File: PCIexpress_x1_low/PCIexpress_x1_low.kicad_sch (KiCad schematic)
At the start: 0 parts

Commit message: working to route 0.8mm pitch bga, probably not practical
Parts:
- added U1: XC7A50T-CSG325, Package_BGA:Xilinx_CSG325, symbol FPGA_Xilinx_Artix7:XC7A50T-CSG325
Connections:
- net PER0_N: now also U1.B1 (MGTPTXN3_216)
- net PER0_P: now also U1.B2 (MGTPTXP3_216)
- net PET0_N: now also U1.G3 (MGTPRXN3_216)
- net PET0_P: now also U1.G4 (MGTPRXP3_216)
- net REFCLK+: now also U1.D6 (MGTREFCLK0P_216)
- net REFCLK-: now also U1.D5 (MGTREFCLK0N_216)
- new net GND: U1.A1 (GND), U1.A11 (GND), U1.A18 (GND), U1.A5 (GND), U1.A7 (GND), U1.A8 (GND), U1.B18 (GND), U1.B3 (GND), U1.B7 (GND), U1.B8 (GND), U1.C15 (GND), U1.C2 (GND), U1.C6 (GND), U1.C7 (GND), U1.D12 (GND), U1.D3 (GND), U1.D4 (GND), U1.D7 (GND), U1.E2 (GND), U1.E6 (GND), U1.E7 (GND), U1.E9 (GND), U1.F10 (GND), U1.F16 (GND), U1.F4 (GND), U1.F6 (GND), U1.G1 (GND), U1.G11 (GND), U1.G13 (GND), U1.G5 (GND), U1.G6 (GND), U1.G7 (GND), U1.G9 (GND), U1.H10 (GND), U1.H12 (GND), U1.H3 (GND), U1.H4 (GND), U1.H5 (GND), U1.H6 (GND), U1.H8 (GND), U1.J1 (GND), U1.J11 (GND), U1.J13 (GND), U1.J17 (GND), U1.J2 (GND), U1.J3 (GND), U1.J7 (GND), U1.K12 (GND), U1.K14 (GND), U1.K4 (GND), U1.K8 (GND), U1.L1 (GND), U1.L11 (GND), U1.L13 (GND), U1.L7 (GND), U1.M12 (GND), U1.M18 (GND), U1.M8 (GND), U1.N11 (GND), U1.N13 (GND), U1.N15 (GND), U1.N5 (GND), U1.N7 (GND), U1.N9 (GND), U1.P12 (GND), U1.P2 (GND), U1.P8 (GND), U1.R9 (GND), U1.T16 (GND), U1.T6 (GND), U1.U13 (GND), U1.U3 (GND), U1.V1 (GND), U1.V10 (GND), U1.V18 (GND)

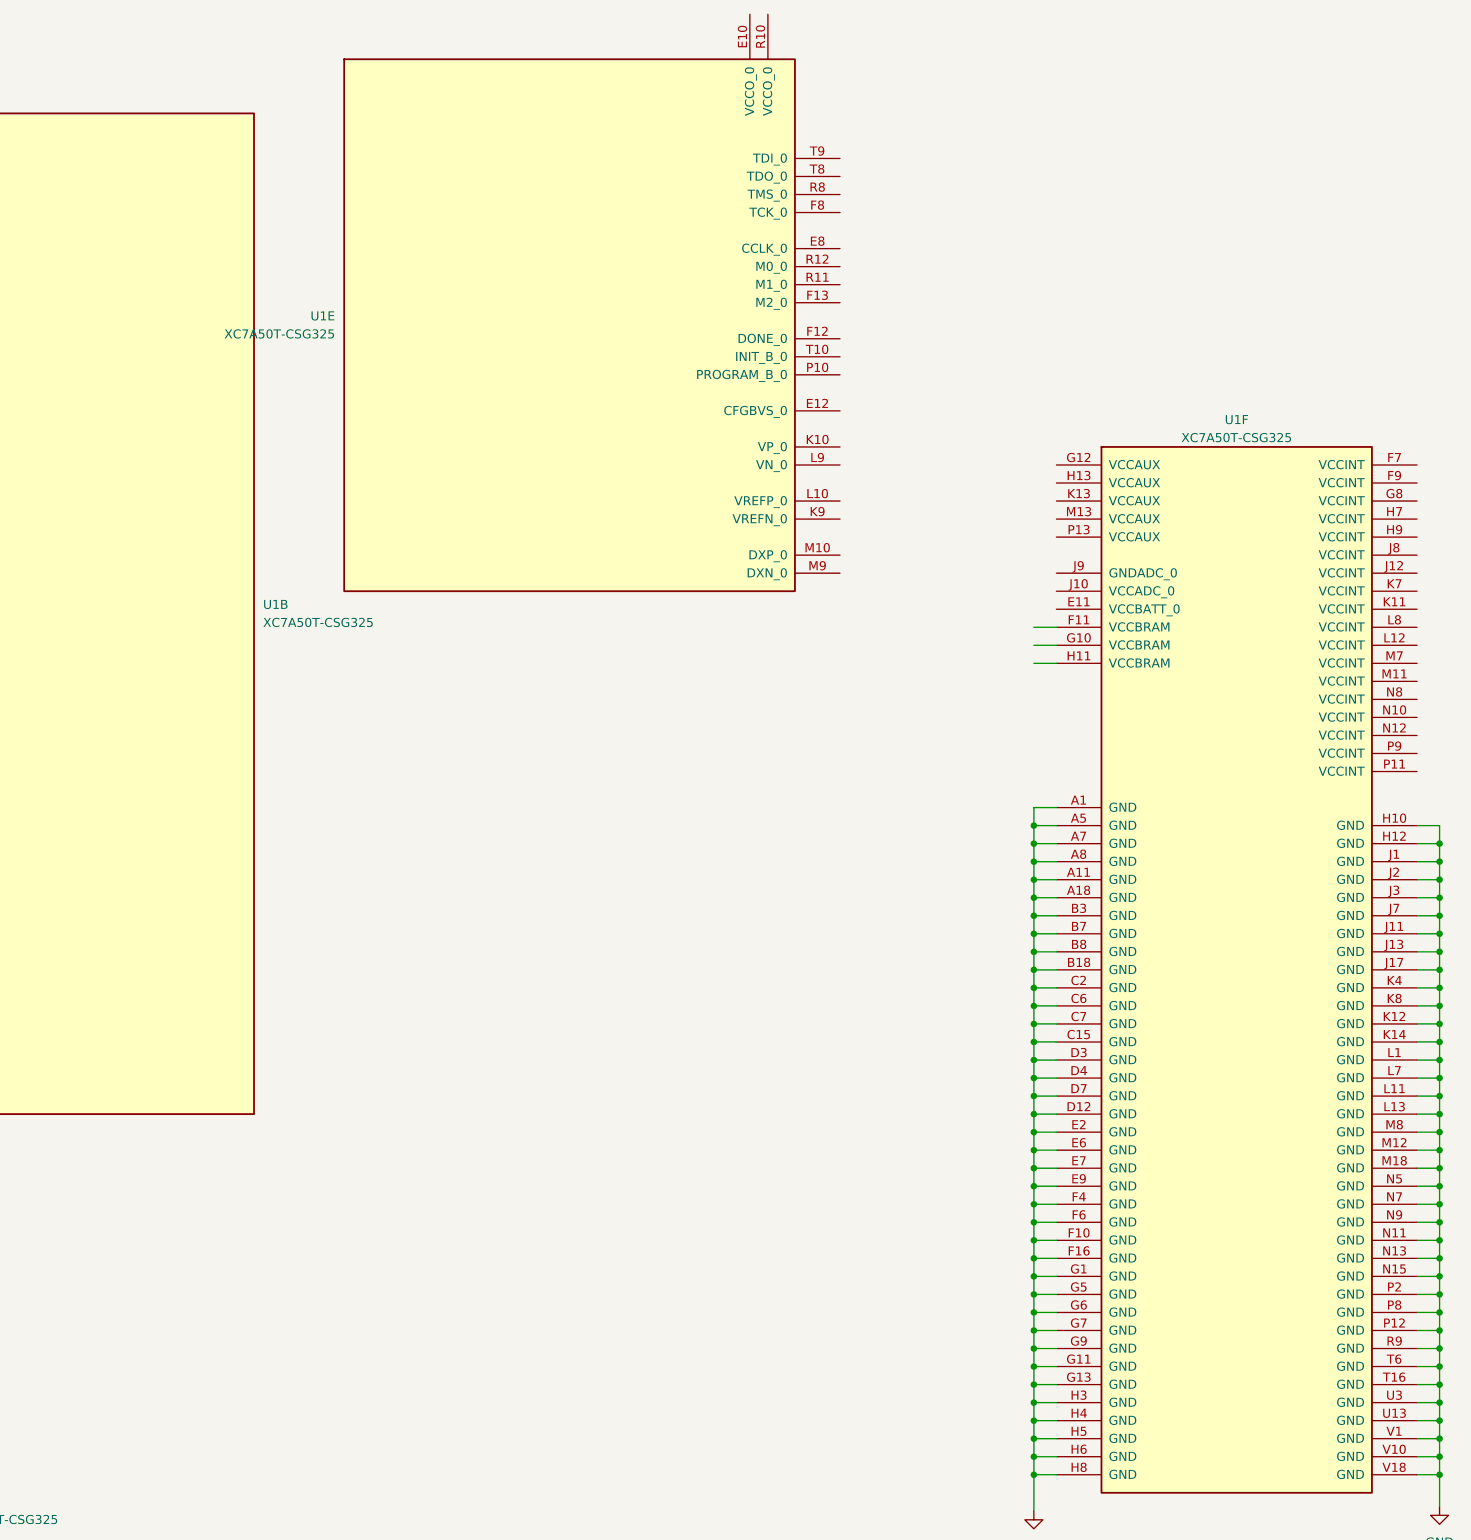
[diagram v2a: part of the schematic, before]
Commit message: looks liket the xilinx csg325 package can route in Oshpark 6 layer stackup
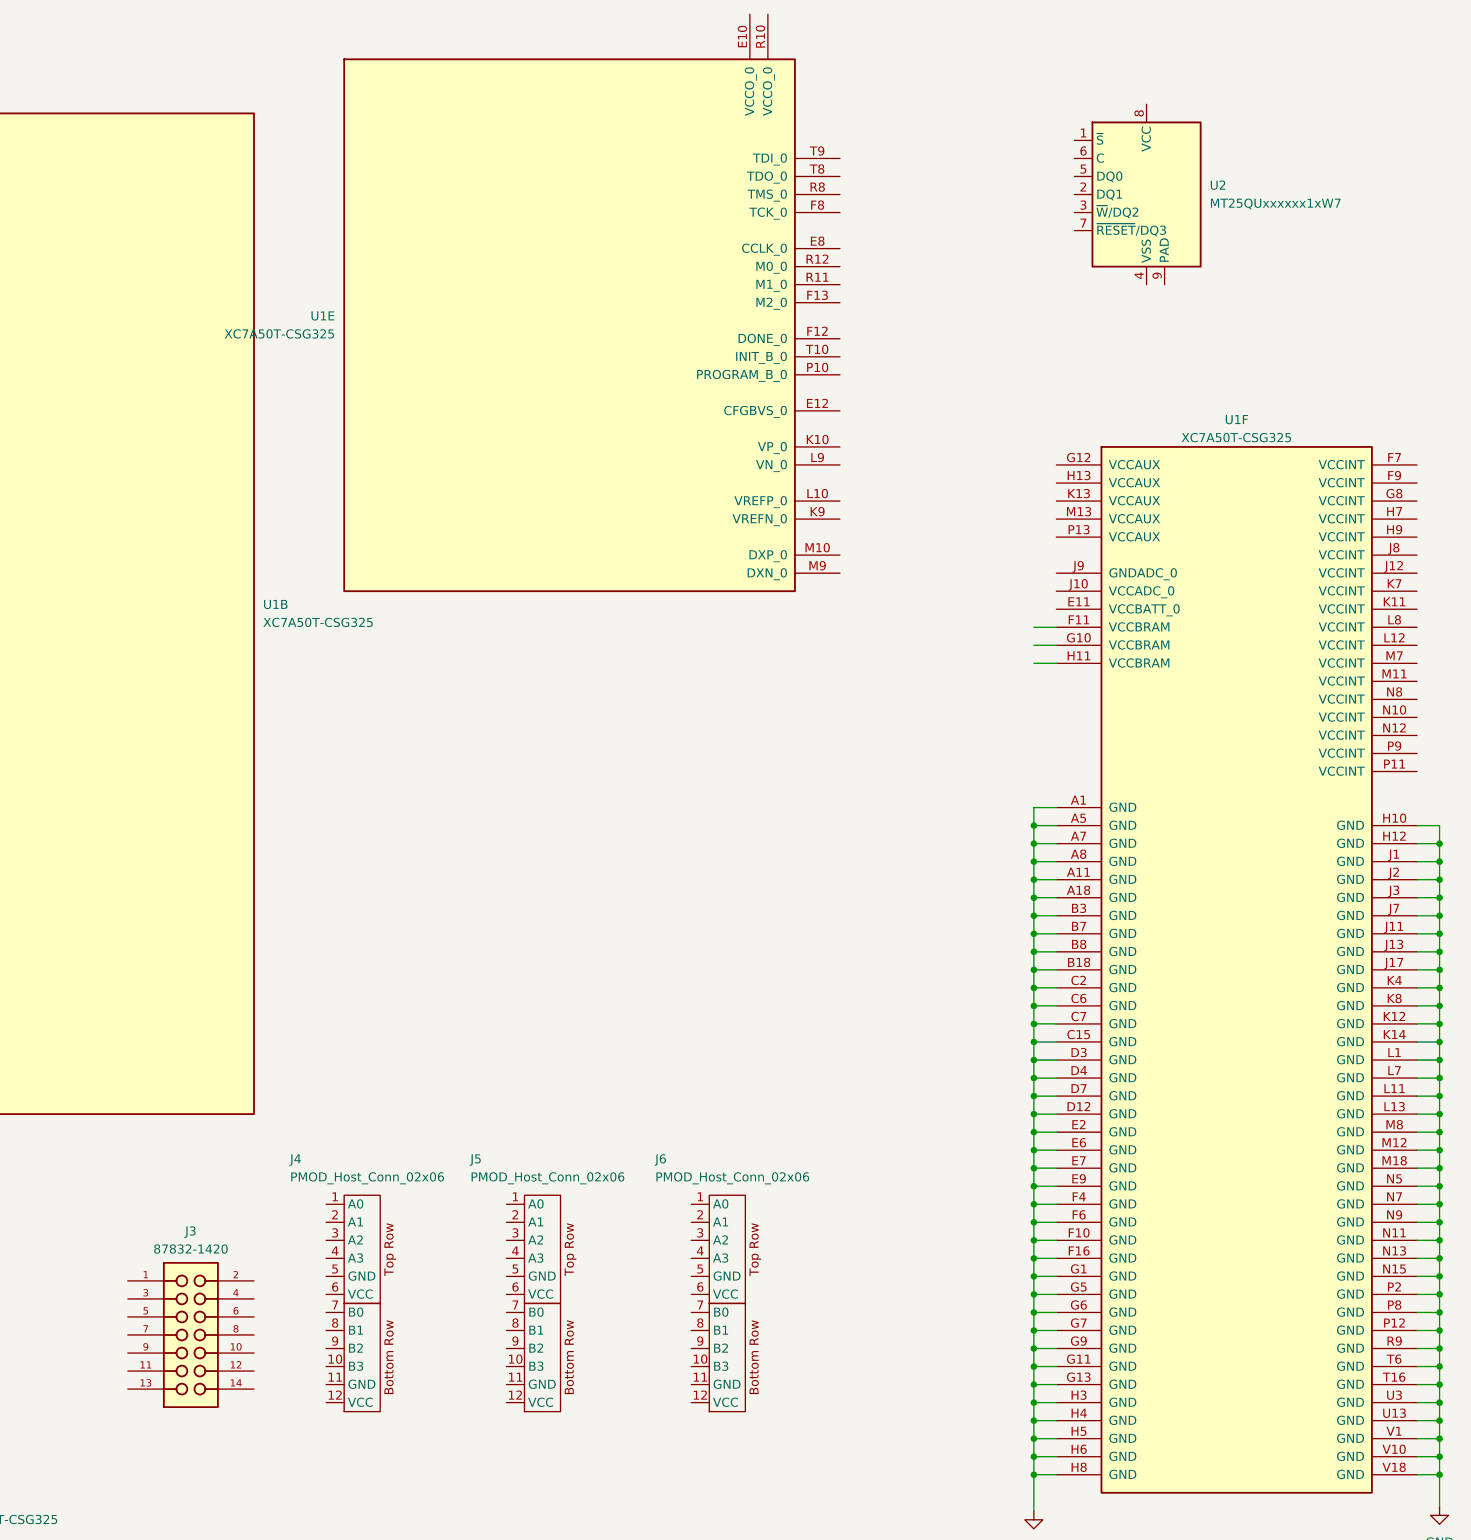
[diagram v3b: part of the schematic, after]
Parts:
- added J3: 87832-1420, pedrolib:MOLEX_87832-1420, symbol pedrolib:87832-1420
- added J4, J5, J6: PMOD_Host_Conn_02x06, pedrolib:PMOD_PinSocket_2x06_P2.54mm_Horizontal, symbol pedrolib:PMOD_Host_Conn_02x06
- added U2: MT25QUxxxxxx1xW7, Package_DFN_QFN:W-PDFN-8-1EP_6x5mm_P1.27mm_EP3x3mm, symbol Memory_Flash:MT25QUxxxxxx1xW7
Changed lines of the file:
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@@
+    )
+  )
+  (symbol (lib_id "pedrolib:PMOD_Host_Conn_02x06") (at 271.78 190.5 0) (unit 1)
+    (in_bom yes) (on_board yes) (dnp no)
+    (property "Reference" "J5" (at 261.62 170.18 0)
+      (effects (font (size 1.27 1.27)) (justify left))
+    )
+    (property "Value" "PMOD_Host_Conn_02x06" (at 261.62 172.72 0)
+      (effects (font (size 1.27 1.27)) (justify left))
+    )
+    (property "Footprint" "pedrolib:PMOD_PinSocket_2x06_P2.54mm_Horizontal" (at 248.92 194.31 0)
+      (effects (font (size 1.27 1.27)) hide)
+    )
+    (property "Datasheet" "" (at 248.92 194.31 0)
+      (effects (font (size 1.27 1.27)) hide)
+    )
+    (pin "1")
+    (pin "10")
+    (pin "11")
+    (pin "12")
+    (pin "2")
+    (pin "3")
+    (pin "4")
+    (pin "5")
+    (pin "6")
+    (pin "7")
+    (pin "8")
+    (pin "9")
+    (instances
+      (project "PCIexpress_x1_low"
+        (path "/b58173cd-28d5-49a4-a789-299fbf6f5cc2"
+          (reference "J5") (unit 1)
+        )
+      )
     )
   )
@@
     )
   )
+  (symbol (lib_id "pedrolib:PMOD_Host_Conn_02x06") (at 246.38 190.5 0) (unit 1)
+    (in_bom yes) (on_board yes) (dnp no)
+    (property "Reference" "J4" (at 236.22 170.18 0)
+      (effects (font (size 1.27 1.27)) (justify left))
+    )
+    (property "Value" "PMOD_Host_Conn_02x06" (at 236.22 172.72 0)
+      (effects (font (size 1.27 1.27)) (justify left))
+    )
+    (property "Footprint" "pedrolib:PMOD_PinSocket_2x06_P2.54mm_Horizontal" (at 223.52 194.31 0)
+      (effects (font (size 1.27 1.27)) hide)
+    )
+    (property "Datasheet" "" (at 223.52 194.31 0)
+      (effects (font (size 1.27 1.27)) hide)
+    )
+    (pin "1")
+    (pin "10")
+    (pin "11")
+    (pin "12")
+    (pin "2")
+    (pin "3")
+    (pin "4")
+    (pin "5")
+    (pin "6")
+    (pin "7")
+    (pin "8")
+    (pin "9")
+    (instances
+      (project "PCIexpress_x1_low"
+        (path "/b58173cd-28d5-49a4-a789-299fbf6f5cc2"
+          (reference "J4") (unit 1)
+        )
+      )
+    )
+  )
   (symbol (lib_id "FPGA_Xilinx_Artix7:XC7A50T-CSG325") (at 275.59 49.53 0) (unit 5)
     (in_bom yes) (on_board yes) (dnp no) (fields_autoplaced)
@@
     )
   )
+  (symbol (lib_id "Memory_Flash:MT25QUxxxxxx1xW7") (at 356.87 34.29 0) (unit 1)
+    (in_bom yes) (on_board yes) (dnp no) (fields_autoplaced)
+    (property "Reference" "U2" (at 365.76 33.02 0)
+      (effects (font (size 1.27 1.27)) (justify left))
+    )
+    (property "Value" "MT25QUxxxxxx1xW7" (at 365.76 35.56 0)
+      (effects (font (size 1.27 1.27)) (justify left))
+    )
+    (property "Footprint" "Package_DFN_QFN:W-PDFN-8-1EP_6x5mm_P1.27mm_EP3x3mm" (at 377.19 31.75 0)
+      (effects (font (size 1.27 1.27)) hide)
+    )
+    (property "Datasheet" "https://media-www.micron.com/-/media/client/global/documents/products/data-sheet/nor-flash/serial-nor/mt25q/die-rev-a/mt25q_qljs_u_256_aba_0.pdf" (at 356.87 16.51 0)
+      (effects (font (size 1.27 1.27)) hide)
+    )
+    (pin "1")
+    (pin "2")
+    (pin "3")
+    (pin "4")
+    (pin "5")
+    (pin "6")
+    (pin "7")
+    (pin "8")
+    (pin "9")
+    (instances
+      (project "PCIexpress_x1_low"
+        (path "/b58173cd-28d5-49a4-a789-299fbf6f5cc2"
+          (reference "U2") (unit 1)
+        )
+      )
+    )
+  )
+  (symbol (lib_id "pedrolib:PMOD_Host_Conn_02x06") (at 297.815 190.5 0) (unit 1)
+    (in_bom yes) (on_board yes) (dnp no)
+    (property "Reference" "J6" (at 287.655 170.18 0)
+      (effects (font (size 1.27 1.27)) (justify left))
+    )
+    (property "Value" "PMOD_Host_Conn_02x06" (at 287.655 172.72 0)
+      (effects (font (size 1.27 1.27)) (justify left))
+    )
+    (property "Footprint" "pedrolib:PMOD_PinSocket_2x06_P2.54mm_Horizontal" (at 274.955 194.31 0)
+      (effects (font (size 1.27 1.27)) hide)
+    )
+    (property "Datasheet" "" (at 274.955 194.31 0)
+      (effects (font (size 1.27 1.27)) hide)
+    )
+    (pin "1")
+    (pin "10")
+    (pin "11")
+    (pin "12")
+    (pin "2")
+    (pin "3")
+    (pin "4")
+    (pin "5")
+    (pin "6")
+    (pin "7")
+    (pin "8")
+    (pin "9")
+    (instances
+      (project "PCIexpress_x1_low"
+        (path "/b58173cd-28d5-49a4-a789-299fbf6f5cc2"
+          (reference "J6") (unit 1)
+        )
+      )
+    )
+  )
   (symbol (lib_id "power:GND") (at 398.145 219.075 0) (unit 1)
     (in_bom yes) (on_board yes) (dnp no) (fields_autoplaced)
@@
         )
       )
+    )
+  )
+  (symbol (lib_id "pedrolib:87832-1420") (at 223.52 194.945 0) (unit 1)
+    (in_bom yes) (on_board yes) (dnp no) (fields_autoplaced)
+    (property "Reference" "J3" (at 222.25 180.34 0)
+      (effects (font (size 1.27 1.27)))
+    )
+    (property "Value" "87832-1420" (at 222.25 182.88 0)
+      (effects (font (size 1.27 1.27)))
+    )
+    (property "Footprint" "pedrolib:MOLEX_87832-1420" (at 222.25 208.915 0)
+      (effects (font (size 1.27 1.27)) (justify bottom) hide)
+    )
+    (property "Datasheet" "" (at 223.52 194.945 0)
+      (effects (font (size 1.27 1.27)) hide)
+    )
+    (property "MANUFACTURER" "MOLEX" (at 223.52 194.945 0)
+      (effects (font (size 1.27 1.27)) (justify bottom) hide)
+    )
+    (pin "1")
+    (pin "10")
+    (pin "11")
+    (pin "12")
+    (pin "13")
+    (pin "14")
+    (pin "2")
+    (pin "3")
+    (pin "4")
+    (pin "5")
+    (pin "6")
+    (pin "7")
+    (pin "8")
+    (pin "9")
+    (instances
+      (project "PCIexpress_x1_low"
+        (path "/b58173cd-28d5-49a4-a789-299fbf6f5cc2"
+          (reference "J3") (unit 1)
+        )
+      )

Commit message: added pmic and config flash
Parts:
- removed U2: MT25QUxxxxxx1xW7, Package_DFN_QFN:W-PDFN-8-1EP_6x5mm_P1.27mm_EP3x3mm, symbol Memory_Flash:MT25QUxxxxxx1xW7
- added U2: LTM4643EY_PBF, pedrolib:BGA77C127P7X11_1500X900X262, symbol pedrolib:LTM4643EY_PBF
- added U3: MX25L3233FM1, Package_SO:SOP-8_3.9x4.9mm_P1.27mm, symbol Memory_Flash:MX25L3233FM1
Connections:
- new net: U2.A1 (VOUT1), U2.A2 (VOUT1), U2.A3 (VOUT1)
- new net: U2.A4 (GND), U2.A5 (GND), U2.B1 (GND), U2.B2 (GND), U2.C5 (GND), U2.D3 (GND), U2.D4 (GND), U2.D5 (GND), U2.E1 (GND), U2.E2 (GND), U2.F5 (GND), U2.G3 (GND), U2.G4 (GND), U2.G5 (GND), U2.H1 (GND), U2.H2 (GND), U2.J5 (GND), U2.K3 (GND), U2.K4 (GND), U2.L1 (GND), U2.L2 (GND)
- new net: U2.B3 (VIN1), U2.B4 (VIN1)
- new net: U2.C1 (VOUT2), U2.D1 (VOUT2), U2.D2 (VOUT2)
- new net: U2.E3 (VIN2), U2.E4 (VIN2)
- new net: U2.F1 (VOUT3), U2.G1 (VOUT3), U2.G2 (VOUT3)
- new net: U2.H3 (VIN3), U2.H4 (VIN3)
- new net: U2.J1 (VOUT4), U2.K1 (VOUT4), U2.K2 (VOUT4)
- new net: U2.L3 (VIN4), U2.L4 (VIN4)
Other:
- company: Author: Luca Anastasio -> Author: HDLguy
- moved on the sheet: J3, J4, J5, J6, U1D

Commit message: threw down some LEDs
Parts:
- added D1, D2, D3, D4, D5, D6, D7, D8: LED, LED_SMD:LED_0603_1608Metric, symbol Device:LED
- added J1: PCIexpress_bracket, PCIexpress:PCIexpress_bracket_low, symbol PCIexpress:PCIexpress_bracket
- added R1, R2, R3, R4, R5, R6, R7, R8: R, Resistor_SMD:R_0603_1608Metric, symbol Device:R
